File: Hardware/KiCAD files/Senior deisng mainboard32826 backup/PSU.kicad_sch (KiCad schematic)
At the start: 33 parts, among them J13 Conn_01x03_Pin, J14 Conn_01x03, J15 Conn_01x03, J26 Conn_01x03_Pin, J28 Conn_01x03, J8 Conn_01x03_Pin, U11 LM2576S-12, U6 LM2576S-12, U7 LM2576S-12

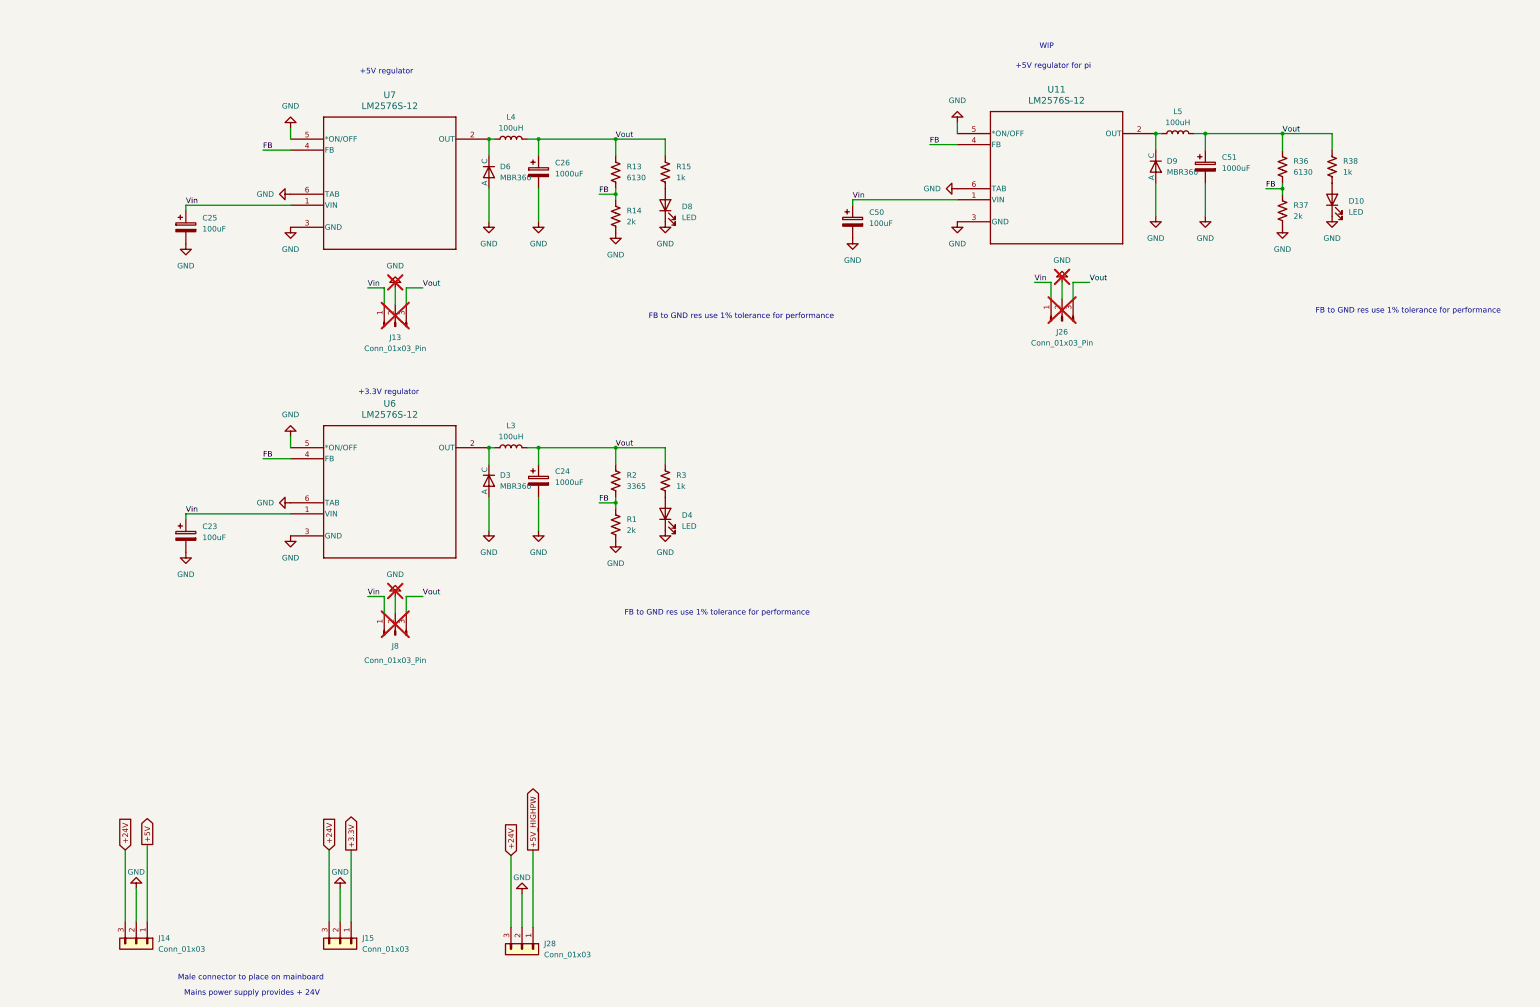
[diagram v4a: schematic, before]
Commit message: New project made to reflect layouts
New project files made in order to generate accurate layouts and create neatness.
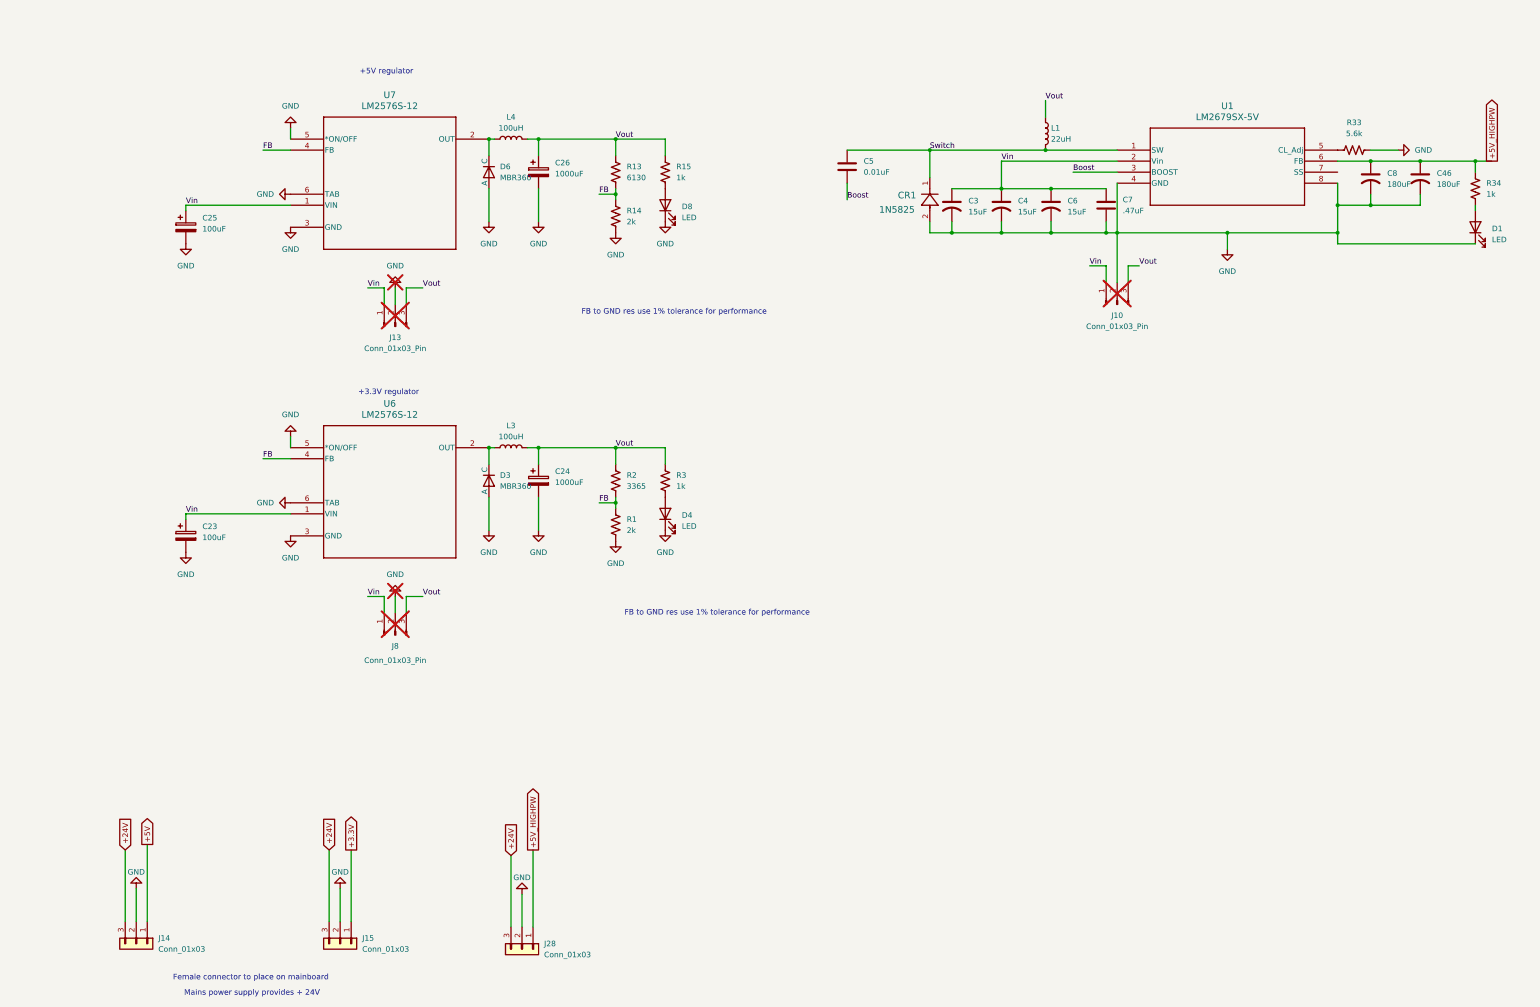
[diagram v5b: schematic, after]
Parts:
- removed C50: 100uF, Capacitor_SMD:CP_Elec_5x3, symbol Device:C_Polarized
- removed C51: 1000uF, Capacitor_SMD:CP_Elec_5x3, symbol Device:C_Polarized
- removed D10: LED, LED_SMD:LED_0603_1608Metric, symbol Device:LED
- removed D9: MBR360, symbol MBR360:Diode
- removed J26: Conn_01x03_Pin, Connector_PinHeader_1.00mm:PinHeader_1x03_P1.00mm_Vertical, symbol Connector:Conn_01x03_Pin
- removed L5: 100uH, Inductor_SMD:L_1206_3216Metric_Pad1.22x1.90mm_HandSolder, symbol Device:L
- removed R36: 6130, symbol Device:R_US
- removed R37: 2k, symbol Device:R_US
- removed R38: 1k, Resistor_SMD:R_1206_3216Metric_Pad1.30x1.75mm_HandSolder, symbol Device:R_US
- removed U11: LM2576S-12, symbol LM2576ADJ:LM2576S-12
- added C3, C4, C6: 15uF, Capacitor_THT:C_Axial_L3.8mm_D2.6mm_P7.50mm_Horizontal, symbol Device:C_US
- added C46, C8: 180uF, Capacitor_THT:C_Radial_D8.0mm_H7.0mm_P3.50mm, symbol Device:C_US
- added C5: 0.01uF, Capacitor_THT:C_Axial_L3.8mm_D2.6mm_P7.50mm_Horizontal, symbol Device:C
- added C7: .47uF, Capacitor_THT:C_Axial_L3.8mm_D2.6mm_P7.50mm_Horizontal, symbol Device:C
- added CR1: 1N5825, symbol 1N5825:1N5825
- added D1: LED, LED_SMD:LED_1206_3216Metric_Pad1.42x1.75mm_HandSolder, symbol Device:LED
- added J10: Conn_01x03_Pin, Connector_PinHeader_2.54mm:PinHeader_1x03_P2.54mm_Vertical, symbol Connector:Conn_01x03_Pin
- added L1: 22uH, Inductor_SMD:L_1206_3216Metric_Pad1.22x1.90mm_HandSolder, symbol Device:L
- added R33: 5.6k, Resistor_SMD:R_1206_3216Metric_Pad1.30x1.75mm_HandSolder, symbol Device:R_US
- added R34: 1k, Resistor_SMD:R_1206_3216Metric_Pad1.30x1.75mm_HandSolder, symbol Device:R_US
- added U1: LM2679SX-5V, LM2679:TS7B, symbol 2026-04-06_04-47-50:LM2679SX-ADJ_NOPB
- D3, D6: footprint (none) -> PCM_Diode_THT_AKL:D_DO-7_DO-204AA_P12.70mm_Horizontal
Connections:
- net +5V_HIGHPW: now also C46.1, C8.1, R34.1, U1.6 (FB)
- net GND: now also C3.2, C4.2, C46.2, C6.2, C7.2, C8.2, CR1.2, D1.1 (K), J10.2 (Pin_2), R33.2, U1.4 (GND), U1.8
- net Vin: now also C3.1, C4.1, C6.1, C7.1, J10.1 (Pin_1), U1.2 (Vin)
- net Vout: now also J10.3 (Pin_3), L1.1
- new net: D1.2 (A), R34.2
- new net: R33.1, U1.5 (CL_Adj)
- new net Boost: C5.2, U1.3 (BOOST)
- new net Switch: C5.1, CR1.1, L1.2, U1.1 (SW)
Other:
- note added: "Female connector to place on mainboard"
- note removed: "+5V regulator for pi"
- note removed: "Male connector to place on mainboard"
- note removed: "WIP"
